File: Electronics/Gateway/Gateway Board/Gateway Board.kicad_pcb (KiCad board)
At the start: 2 copper layers, 110 parts, among them IC1 STM32H723ZGT6, IC2 TJA1057GT/3, IC3 TJA1057GT/3, IC4 TJA1057GT/3, IC5 TPS54295PWPR, IC6 LAN8742A-CZ-TR, J1 TYPE-C-31-M-12, J10 Conn_01x02_Pin, J11 Conn_01x02_Pin, J2 Screw_Terminal_01x02, J3 TC2030, J4 HR913129A, J5 Screw_Terminal_01x02, J6 Screw_Terminal_01x02, J7 MEM2075-00-140-01-A, J8 Screw_Terminal_01x02, J9 Conn_01x02_Pin, SW1 SW_DIP_x02, U1 USBLC6-4SC6-ES, U2 USBLC6-4SC6-ES, U3 USBLC6-4SC6-ES, X1 25MHz_Clock, X2 32.768kHz_Clock, X3 25MHz_Clock

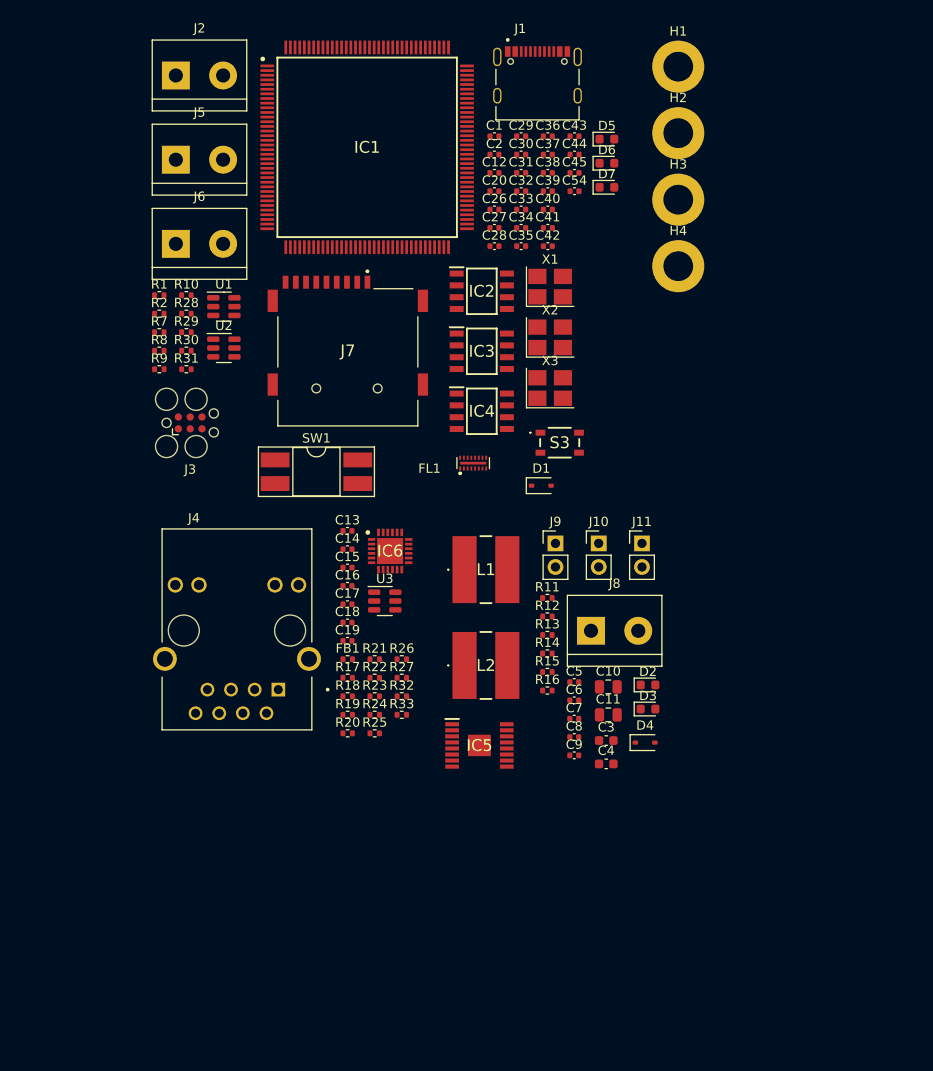
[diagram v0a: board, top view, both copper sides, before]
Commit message: Gateway board layout complete and routing begun
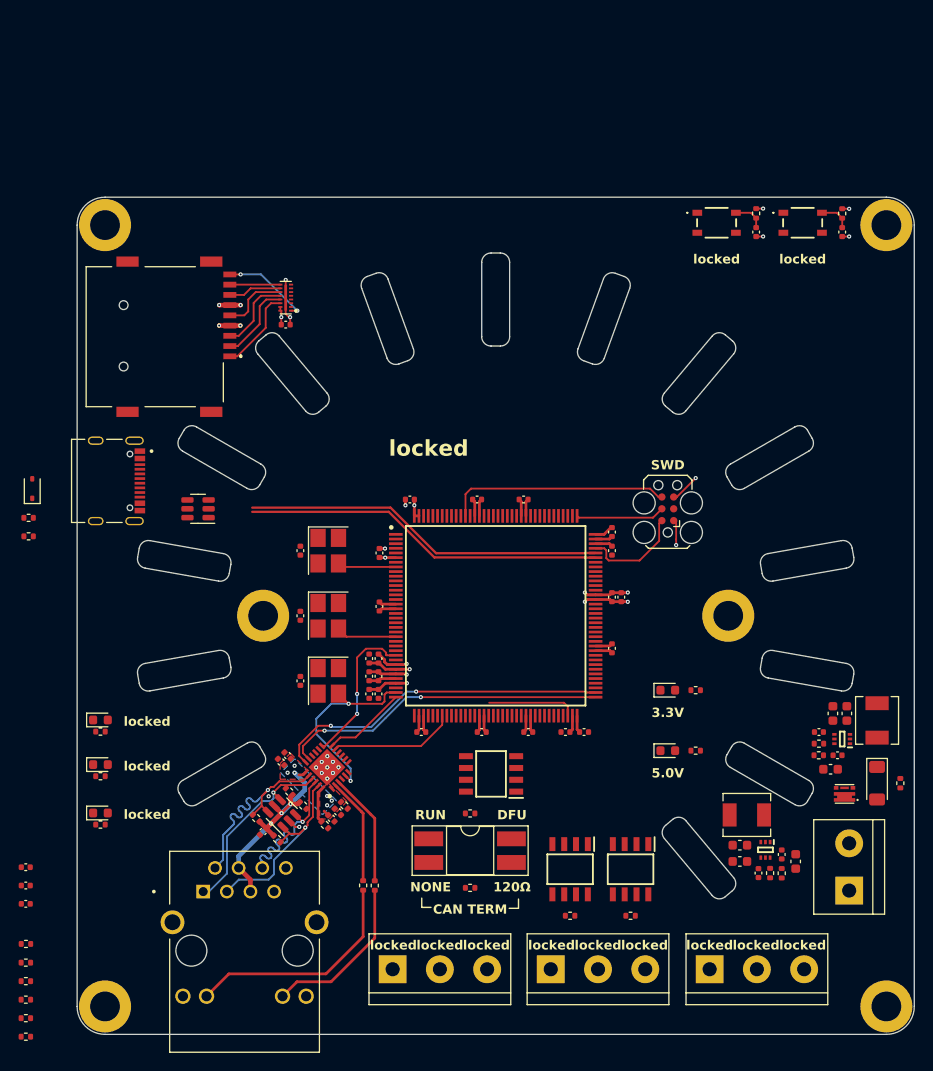
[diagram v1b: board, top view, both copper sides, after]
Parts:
- removed C1, C12, C13, C14, C18, C19, C2, C28, C30, C32, C33, C34, C35, C36, C37, C39, C40, C41, C42, C43, C44, C7, C8: 100n, Capacitor_SMD:C_0402_1005Metric
- removed C10, C11: 47u, Capacitor_SMD:C_0805_2012Metric
- removed C15, C20, C38, C45: 10u, Capacitor_SMD:C_0402_1005Metric
- removed C16, C29, C31, C9: 1u, Capacitor_SMD:C_0402_1005Metric
- removed C17: 470p, Capacitor_SMD:C_0402_1005Metric
- removed C26, C27: 2u2, Capacitor_SMD:C_0402_1005Metric
- removed C3, C4: 10u, Capacitor_SMD:C_0603_1608Metric
- removed C5, C54, C6: 10n, Capacitor_SMD:C_0402_1005Metric
- removed D1, D4: BAT760-115, Diode_SMD:D_SOD-323
- removed D2, D3, D6: Green, LED_SMD:LED_0603_1608Metric
- removed D5: Red, LED_SMD:LED_0603_1608Metric
- removed D7: Blue, LED_SMD:LED_0603_1608Metric
- removed FB1: 120R@100MHz, Resistor_SMD:R_0402_1005Metric
- removed FL1: EMIF06-MSD02N16, footprints:EMIF06MSD02N16
- removed H1, H2, H3, H4: MountingHole_Pad, MountingHole:MountingHole_3.2mm_M3_DIN965_Pad
- removed IC1: STM32H723ZGT6, MSL Footprints:QFP50P2200X2200X160-144N
- removed IC2, IC3, IC4: TJA1057GT/3, MSL Footprints:SOIC127P600X175-8N
- removed IC5: TPS54295PWPR, MSL Footprints:SOP65P640X120-17N
- removed IC6: LAN8742A-CZ-TR, MSL Footprints:QFN50P400X400X100-25N-D
- removed J1: TYPE-C-31-M-12, MSL Footprints:HRO_TYPE-C-31-M-12
- removed J10, J11, J9: Conn_01x02_Pin, Connector_PinHeader_2.54mm:PinHeader_1x02_P2.54mm_Vertical
- removed J2, J5, J6, J8: Screw_Terminal_01x02, TerminalBlock:TerminalBlock_bornier-2_P5.08mm
- removed J3: TC2030, Connector:Tag-Connect_TC2030-IDC-FP_2x03_P1.27mm_Vertical
- removed J4: HR913129A, MSL Footprints:HANRUN_HR913129A
- removed J7: MEM2075-00-140-01-A, MSL Footprints:MEM20750014001A
- removed L1: 3u3, MSL Footprints:29332C
- removed L2: 2u2, MSL Footprints:29222C
- removed R1, R2, R9: 120R, Resistor_SMD:R_0402_1005Metric
- removed R10, R14, R22, R25, R26, R27, R28, R33: 10k, Resistor_SMD:R_0402_1005Metric
- removed R11: 124k, Resistor_SMD:R_0402_1005Metric
- removed R12: 22k1, Resistor_SMD:R_0402_1005Metric
- removed R13: 33k, Resistor_SMD:R_0402_1005Metric
- removed R15: 2k2, Resistor_SMD:R_0402_1005Metric
- removed R16, R29, R30, R31, R32: 1k5, Resistor_SMD:R_0402_1005Metric
- removed R17, R18, R19, R20: 49R9, Resistor_SMD:R_0402_1005Metric
- removed R21: 12k1, Resistor_SMD:R_0402_1005Metric
- removed R23, R24: 330R, Resistor_SMD:R_0402_1005Metric
- removed R7, R8: 5k1, Resistor_SMD:R_0402_1005Metric
- removed S3: TS20-42-25-WT-160-SMT-TR, MSL Footprints:TS204225WT160SMTTRMSL
- removed SW1: SW_DIP_x02, Package_DIP:DIP-4_W8.89mm_SMDSocket_LongPads
- removed U1, U2, U3: USBLC6-4SC6-ES, Package_TO_SOT_SMD:SOT-23-6
- removed X1, X3: 25MHz_Clock, Oscillator:Oscillator_SMD_Abracon_ASE-4Pin_3.2x2.5mm_HandSoldering
- removed X2: 32.768kHz_Clock, Oscillator:Oscillator_SMD_Abracon_ASE-4Pin_3.2x2.5mm_HandSoldering
- added C201: 22u, Capacitor_SMD:C_0603_1608Metric, F.Cu at (177.2, 126.4)
- added C202: 22u, Capacitor_SMD:C_0603_1608Metric, F.Cu at (181.0, 116.5)
- added C203: 100n, Capacitor_SMD:C_0402_1005Metric, F.Cu at (175.8, 125.7)
- added C204: 100n, Capacitor_SMD:C_0402_1005Metric, F.Cu at (181.8, 115.0)
- added C205: 100n, Capacitor_SMD:C_0402_1005Metric, F.Cu at (173.2, 127.7)
- added C206: 100n, Capacitor_SMD:C_0402_1005Metric, F.Cu at (179.8, 112.5)
- added C207: 22u, Capacitor_SMD:C_0603_1608Metric, F.Cu at (171.2, 124.7)
- added C208: 22u, Capacitor_SMD:C_0603_1608Metric, F.Cu at (182.8, 110.5)
- added C209: 22u, Capacitor_SMD:C_0603_1608Metric, F.Cu at (171.2, 126.4)
- added C210: 22u, Capacitor_SMD:C_0603_1608Metric, F.Cu at (181.2, 110.5)
- added C301: 100n, Capacitor_SMD:C_0402_1005Metric, F.Cu at (124.0, 93.0)
- added C302: 100n, Capacitor_SMD:C_0402_1005Metric, F.Cu at (124.0, 100.0)
- added C303: 100n, Capacitor_SMD:C_0402_1005Metric, F.Cu at (124.0, 107.0)
- added C304: 10n, Capacitor_SMD:C_0402_1005Metric, F.Cu at (182.2, 58.8)
- added C305: 100n, Capacitor_SMD:C_0402_1005Metric, F.Cu at (132.4, 106.5)
- added C306: 1u, Capacitor_SMD:C_0402_1005Metric, F.Cu at (131.4, 106.5)
- added C307: 100n, Capacitor_SMD:C_0402_1005Metric, F.Cu at (135.8, 87.5)
- added C308: 100n, Capacitor_SMD:C_0402_1005Metric, F.Cu at (132.4, 108.4)
- added C309: 100n, Capacitor_SMD:C_0402_1005Metric, F.Cu at (157.5, 98.0)
- added C310: 1u, Capacitor_SMD:C_0402_1005Metric, F.Cu at (131.4, 108.4)
- added C311: 100n, Capacitor_SMD:C_0402_1005Metric, F.Cu at (132.5, 93.2)
- added C312: 100n, Capacitor_SMD:C_0402_1005Metric, F.Cu at (132.5, 99.0)
- added C313: 100n, Capacitor_SMD:C_0402_1005Metric, F.Cu at (137.0, 112.5)
- added C314: 100n, Capacitor_SMD:C_0402_1005Metric, F.Cu at (132.4, 104.6)
- added C315: 10u, Capacitor_SMD:C_0402_1005Metric, F.Cu at (158.5, 98.0)
- added C316: 100n, Capacitor_SMD:C_0402_1005Metric, F.Cu at (157.5, 91.0)
- added C317: 100n, Capacitor_SMD:C_0402_1005Metric, F.Cu at (154.5, 112.5)
- added C318: 100n, Capacitor_SMD:C_0402_1005Metric, F.Cu at (148.5, 112.5)
- added C319: 100n, Capacitor_SMD:C_0402_1005Metric, F.Cu at (143.5, 112.5)
- added C320: 100n, Capacitor_SMD:C_0402_1005Metric, F.Cu at (143.0, 87.5)
- added C321: 100n, Capacitor_SMD:C_0402_1005Metric, F.Cu at (148.0, 87.5)
- added C322: 10u, Capacitor_SMD:C_0402_1005Metric, F.Cu at (131.4, 104.6)
- added C323: 2u2, Capacitor_SMD:C_0402_1005Metric, F.Cu at (152.5, 112.5)
- added C324: 2u2, Capacitor_SMD:C_0402_1005Metric, F.Cu at (157.5, 93.0)
- added C325: 10u, Capacitor_SMD:C_0402_1005Metric, F.Cu at (122.4, 68.7)
- added C326: 10n, Capacitor_SMD:C_0402_1005Metric, F.Cu at (173.0, 58.8)
- added C327: 100n, Capacitor_SMD:C_0402_1005Metric, F.Cu at (157.5, 103.5)
- added C401: 100n, Capacitor_SMD:C_0402_1005Metric, F.Cu at (94.5, 127.0)
- added C402: 1u, Capacitor_SMD:C_0402_1005Metric, F.Cu at (94.5, 129.0)
- added C403: 470p, Capacitor_SMD:C_0402_1005Metric, F.Cu at (94.5, 131.0)
- added C404: 100n, Capacitor_SMD:C_0402_1005Metric, F.Cu at (121.9, 115.7)
- added C405: 100n, Capacitor_SMD:C_0402_1005Metric, F.Cu at (127.3, 121.8)
- added C406: 100n, Capacitor_SMD:C_0402_1005Metric, F.Cu at (122.6, 115.0)
- added C407: 10u, Capacitor_SMD:C_0402_1005Metric, F.Cu at (128.0, 121.1)
- added C408: 100n, Capacitor_SMD:C_0402_1005Metric, F.Cu at (120.0, 123.2)
- added D201: GREEN, LED_SMD:LED_0603_1608Metric, F.Cu at (163.5, 114.5)
- added D202: GREEN, LED_SMD:LED_0603_1608Metric, F.Cu at (163.5, 108.0)
- added D204: ZMM10V, Diode_SMD:D_MiniMELF, F.Cu at (186.0, 118.0)
- added D301: Red, LED_SMD:LED_0603_1608Metric, F.Cu at (102.5, 116.0)
- added D302: Green, LED_SMD:LED_0603_1608Metric, F.Cu at (102.5, 111.2)
- added D303: Blue, LED_SMD:LED_0603_1608Metric, F.Cu at (102.5, 121.2)
- added D304: BAT760-115, Diode_SMD:D_SOD-323, F.Cu at (95.2, 86.3)
- added FB401: 120R@100MHz, Resistor_SMD:R_0402_1005Metric, F.Cu at (128.7, 120.4)
- added FL301: EMIF06-MSD02N16, MSL Footprints:EMIF06MSD02N16, F.Cu at (122.6, 65.8)
- added G***: LOGO, MSL Footprints:ICRS_50mm, B.Cu at (145.0, 100.0)
- added H101: MountingHole_Pad, MountingHole:MountingHole_3.2mm_M3_DIN965_Pad, F.Cu at (103.0, 58.0)
- added H102: MountingHole_Pad, MountingHole:MountingHole_3.2mm_M3_DIN965_Pad, F.Cu at (103.0, 142.0)
- added H103: MountingHole_Pad, MountingHole:MountingHole_3.2mm_M3_DIN965_Pad, F.Cu at (187.0, 58.0)
- added H104: MountingHole_Pad, MountingHole:MountingHole_3.2mm_M3_DIN965_Pad, F.Cu at (187.0, 142.0)
- added H105: MountingHole_Pad, MountingHole:MountingHole_3.2mm_M3_DIN965_Pad, F.Cu at (120.0, 100.0)
- added H106: MountingHole_Pad, MountingHole:MountingHole_3.2mm_M3_DIN965_Pad, F.Cu at (170.0, 100.0)
- added IC201: TPS563202DRLR, MSL Footprints:SOTFL50P160X60-6N, F.Cu at (174.0, 125.2)
- added IC202: TPS563202DRLR, MSL Footprints:SOTFL50P160X60-6N, F.Cu at (182.2, 113.2)
- added IC301: STM32H723ZGT6, MSL Footprints:QFP50P2200X2200X160-144N, F.Cu at (145.0, 100.0)
- added IC302: TJA1057GT/3, MSL Footprints:SOIC127P600X175-8N, F.Cu at (144.5, 117.0)
- added IC303: TJA1057GT/3, MSL Footprints:SOIC127P600X175-8N, F.Cu at (153.0, 127.2)
- added IC304: TJA1057GT/3, MSL Footprints:SOIC127P600X175-8N, F.Cu at (159.5, 127.2)
- added IC401: LAN8742A-CZ-TR, MSL Footprints:QFN50P400X400X100-25N-D, F.Cu at (126.9, 116.3)
- added J201: Pluggable_Terminal_01x02, MSL Footprints:Pluggable_terminal-2_P5.08mm, F.Cu at (183.0, 129.5)
- added J301: TC2030, MSL Footprints:Tag-Connect_TC2030-IDC-FP_2x03_P1.27mm_Vertical, F.Cu at (163.5, 88.5)
- added J302: MEM2075-00-140-01-A, MSL Footprints:MEM20750014001A, F.Cu at (108.7, 70.0)
- added J303: TYPE-C-31-M-12, MSL Footprints:HRO_TYPE-C-31-M-12, F.Cu at (102.0, 85.5)
- added J304: Pluggable_Terminal_01x03, MSL Footprints:Pluggable_terminal-3_P5.08mm, F.Cu at (133.9, 138.0)
- added J305: Pluggable_Terminal_01x03, MSL Footprints:Pluggable_terminal-3_P5.08mm, F.Cu at (150.9, 138.0)
- added J306: Pluggable_Terminal_01x03, MSL Footprints:Pluggable_terminal-3_P5.08mm, F.Cu at (168.0, 138.0)
- added J401: HR913129A, MSL Footprints:HANRUN_HR913129A, F.Cu at (118.0, 136.0)
- added L201: 4u7, Inductor_SMD:L_Chilisin_BMRA00040420, F.Cu at (172.0, 121.4)
- added L202: 3u3, Inductor_SMD:L_Chilisin_BMRA00040420, F.Cu at (186.0, 111.2)
- added Q201: DMP3028LFDE, MSL Footprints:DMP2066UFDE7, F.Cu at (182.5, 119.2)
- added R201: 52k, Resistor_SMD:R_0402_1005Metric, F.Cu at (174.5, 127.7)
- added R202: 10k, Resistor_SMD:R_0402_1005Metric, F.Cu at (175.8, 127.7)
- added R203: 31k, Resistor_SMD:R_0402_1005Metric, F.Cu at (179.8, 113.8)
- added R204: 10k, Resistor_SMD:R_0402_1005Metric, F.Cu at (179.7, 115.0)
- added R205: 2k2, Resistor_SMD:R_0402_1005Metric, F.Cu at (166.5, 114.5)
- added R206: 1k5, Resistor_SMD:R_0402_1005Metric, F.Cu at (166.5, 108.0)
- added R207: 4k7, Resistor_SMD:R_0402_1005Metric, F.Cu at (188.5, 118.0)
- added R301: 1k5, Resistor_SMD:R_0402_1005Metric, F.Cu at (102.5, 117.2)
- added R302: 120R, Resistor_SMD:R_0402_1005Metric, F.Cu at (142.2, 129.2)
- added R303: 1k5, Resistor_SMD:R_0402_1005Metric, F.Cu at (102.5, 112.5)
- added R304: 1k5, Resistor_SMD:R_0402_1005Metric, F.Cu at (102.5, 122.5)
- added R305: 10k, Resistor_SMD:R_0402_1005Metric, F.Cu at (182.2, 56.8)
- added R306: 10k, Resistor_SMD:R_0402_1005Metric, F.Cu at (142.2, 121.2)
- added R307: 120R, Resistor_SMD:R_0402_1005Metric, F.Cu at (153.0, 132.2)
- added R308: 5k1, Resistor_SMD:R_0402_1005Metric, F.Cu at (94.8, 89.5)
- added R309: 5k1, Resistor_SMD:R_0402_1005Metric, F.Cu at (94.8, 91.5)
- added R310: 120R, Resistor_SMD:R_0402_1005Metric, F.Cu at (159.5, 132.2)
- added R311: 10k, Resistor_SMD:R_0402_1005Metric, F.Cu at (173.0, 56.7)
- added R401: 10k, Resistor_SMD:R_0402_1005Metric, F.Cu at (94.5, 135.3)
- added R402: 10k, Resistor_SMD:R_0402_1005Metric, F.Cu at (94.5, 137.3)
- added R403: 10k, Resistor_SMD:R_0402_1005Metric, F.Cu at (94.5, 139.3)
- added R404: 10k, Resistor_SMD:R_0402_1005Metric, F.Cu at (94.5, 141.3)
- added R405: 1k5, Resistor_SMD:R_0402_1005Metric, F.Cu at (94.5, 143.3)
- added R406: 10k, Resistor_SMD:R_0402_1005Metric, F.Cu at (94.5, 145.2)
- added R407: 12k1, Resistor_SMD:R_0402_1005Metric, F.Cu at (126.6, 122.5)
- added R408: 49R9, Resistor_SMD:R_0402_1005Metric, F.Cu at (122.8, 118.9)
- added R409: 49R9, Resistor_SMD:R_0402_1005Metric, F.Cu at (119.2, 121.8)
- added R410: 49R9, Resistor_SMD:R_0402_1005Metric, F.Cu at (121.5, 124.0)
- added R411: 49R9, Resistor_SMD:R_0402_1005Metric, F.Cu at (124.3, 120.4)
- added R412: 330R, Resistor_SMD:R_0402_1005Metric, F.Cu at (130.8, 129.0)
- added R413: 330R, Resistor_SMD:R_0402_1005Metric, F.Cu at (132.0, 129.0)
- added S301: TS20-42-25-WT-160-SMT-TR, MSL Footprints:TS204225WT160SMTTRMSL, F.Cu at (178.0, 57.8)
- added S302: TS20-42-25-WT-160-SMT-TR, MSL Footprints:TS204225WT160SMTTRMSL, F.Cu at (168.8, 57.8)
- added SW301: SW_DIP_x02, Package_DIP:DIP-4_W8.89mm_SMDSocket_LongPads, F.Cu at (142.2, 125.2)
- added U302: USBLC6-4SC6-ES, Package_TO_SOT_SMD:SOT-23-6, F.Cu at (113.0, 88.5)
- added U401: USBLC6-4SC6-ES, Package_TO_SOT_SMD:SOT-23-6, F.Cu at (122.0, 121.2)
- added X301: 50MHz_Clock, Oscillator:Oscillator_SMD_Abracon_ASE-4Pin_3.2x2.5mm_HandSoldering, F.Cu at (127.0, 107.0)
- added X302: 25MHz_Clock, Oscillator:Oscillator_SMD_Abracon_ASE-4Pin_3.2x2.5mm_HandSoldering, F.Cu at (127.0, 100.0)
- added X303: 32.768kHz_Clock, Oscillator:Oscillator_SMD_Abracon_ASE-4Pin_3.2x2.5mm_HandSoldering, F.Cu at (127.0, 93.0)
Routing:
- net +3.3V: track 0.00 -> 43.2 mm, vias 0 -> 12
- net GND: track 0.00 -> 42.2 mm, vias 0 -> 24
- net USB_DP: track 0.00 -> 39.0 mm
- net USB_DN: track 0.00 -> 39.0 mm
- net ETH_TXD1: track 0.00 -> 36.6 mm, vias 0 -> 2
- net ETH_TXD0: track 0.00 -> 35.3 mm, vias 0 -> 2
- net +3.3VA: track 0.00 -> 27.2 mm, vias 0 -> 9
- net /Ethernet/G_K: track 0.00 -> 24.5 mm
- net SWO: track 0.00 -> 24.1 mm
- net /Ethernet/TXN: track 0.00 -> 23.9 mm, vias 0 -> 1
- net /Ethernet/RXP: track 0.00 -> 21.8 mm, vias 0 -> 1
- net ETH_REF_CLK: track 0.00 -> 20.7 mm, vias 0 -> 2
- net /Ethernet/TXP: track 0.00 -> 20.6 mm, vias 0 -> 1
- net /Ethernet/RXN: track 0.00 -> 17.9 mm, vias 0 -> 1
- net /Ethernet/Y_K: track 0.00 -> 17.6 mm
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- added copper zone on B.Cu, net +3.3VA
- added copper zone on F.Cu, net +3.3VA
- added copper zone on In1.Cu, net GND
- added copper zone on In2.Cu, net GND
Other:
- board outline added: 90 x 90 mm
- copper layers 2 -> 4
- board text added: "120Ω"
- board text added: "3.3V"
- board text added: "5.0V"
- board text added: "CAN TERM"
- board text added: "DFU"
- board text added: "NONE"
- board text added: "RUN"
- board text added: "SWD"
- board text added: "locked"

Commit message: Sensor hub board done
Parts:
- added C1: 100n, Capacitor_SMD:C_0402_1005Metric, F.Cu at (140.2, 115.8)
- added C2: 100n, Capacitor_SMD:C_0402_1005Metric, F.Cu at (148.8, 117.0)
- added C3: 100n, Capacitor_SMD:C_0402_1005Metric, F.Cu at (150.5, 131.5)
- added C4: 100n, Capacitor_SMD:C_0402_1005Metric, F.Cu at (153.0, 123.0)
- added C5: 100n, Capacitor_SMD:C_0402_1005Metric, F.Cu at (157.0, 131.5)
- added C6: 100n, Capacitor_SMD:C_0402_1005Metric, F.Cu at (159.5, 123.0)
- added G***: LOGO, MSL Footprints:DC_logo_4mm, B.Cu at (187.3, 129.7)
- moved R405 49.8 mm to (132.2, 110.7)
- moved R404 49.0 mm to (134.5, 112.9)
- moved R403 47.3 mm to (135.7, 116.0), turned to 90 degrees
- moved R406 45.4 mm to (123.9, 110.6), turned to -135 degrees
- moved R402 44.9 mm to (133.1, 114.3), turned to -90 degrees
- moved R401 42.6 mm to (130.8, 113.0)
- moved C402 38.6 mm to (131.2, 117.1), turned to -45 degrees
- moved C401 38.6 mm to (130.8, 114.0), turned to 180 degrees
- moved C403 38.4 mm to (130.5, 117.8), turned to -45 degrees
- moved R306 33.9 mm to (138.7, 87.5)
- moved R308 18.5 mm to (113.0, 86.0)
- moved R309 18.2 mm to (113.0, 91.0)
- moved D304 11.1 mm to (103.5, 93.6)
- moved R302 3.25 mm to (139.0, 129.2)
- moved SW301 3.25 mm to (139.0, 125.2)
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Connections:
- IC301 pad 10: unconnected-(IC301-PF0-Pad10) -> LEDG
- IC301 pad 11: unconnected-(IC301-PF1-Pad11) -> LEDR
- IC301 pad 12: unconnected-(IC301-PF2-Pad12) -> LEDB
- IC301 pad 123: unconnected-(IC301-PD7-Pad123) -> BTN
- IC301 pad 13: unconnected-(IC301-PF3-Pad13) -> ETH_RST
- IC301 pad 14: unconnected-(IC301-PF4-Pad14) -> ETH_INT
- IC301 pad 47: unconnected-(IC301-PB1-Pad47) -> SILENT1
- IC301 pad 64: unconnected-(IC301-PE11-Pad64) -> SILENT2
- IC301 pad 65: unconnected-(IC301-PE12-Pad65) -> SILENT3
- J302 pad 10: GND -> unconnected-(J302-MP1-Pad10)
- J302 pad 11: GND -> unconnected-(J302-MP2-Pad11)
- J302 pad 12: GND -> unconnected-(J302-MP3-Pad12)
- J302 pad 13: GND -> unconnected-(J302-MP4-Pad13)
- J303 pad S2: unconnected-(J303-SHIELD-PadS1) -> unconnected-(J303-SHIELD-PadS2)
- J303 pad S3: unconnected-(J303-SHIELD-PadS1) -> unconnected-(J303-SHIELD-PadS3)
- J303 pad S4: unconnected-(J303-SHIELD-PadS1) -> unconnected-(J303-SHIELD-PadS4)
- R405 pad 2: ETH_MDC -> ETH_MDIO
- U302 pad 1: /Microcontroller/CC1 -> /Microcontroller/CC2
- U302 pad 3: /Microcontroller/CC2 -> /Microcontroller/CC1
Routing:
- net VIN: track 0.00 -> 150.3 mm, vias 0 -> 8
- net NRST: track 3.43 -> 95.2 mm, vias 0 -> 2
- net +3.3V: track 43.2 -> 119.7 mm, vias 12 -> 45
- net GND: track 42.2 -> 114.9 mm, vias 24 -> 97
- net SDMMC1_DAT0: track 0.00 -> 54.7 mm, vias 0 -> 2
- net SDMMC1_DAT1: track 0.00 -> 54.5 mm, vias 0 -> 2
- net LEDB: track 0.00 -> 53.1 mm
- net CAN_RX2: track 0.00 -> 52.7 mm, vias 0 -> 2
- net SDMMC1_CD: track 9.55 -> 61.0 mm, vias 2 -> 5
- net SDMMC1_CLK: track 0.00 -> 50.5 mm
- net CAN_TX2: track 0.00 -> 48.9 mm, vias 0 -> 2
- net LEDR: track 0.00 -> 48.3 mm
- net CAN_TX3: track 0.00 -> 48.2 mm, vias 0 -> 2
- net SDMMC1_DAT3: track 0.00 -> 48.2 mm
- net CAN_RX3: track 0.00 -> 47.2 mm, vias 0 -> 2
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- added copper zone on B.Cu, net +3.3V
- added copper zone on F.Cu, net +3.3V
- added copper zone on B.Cu, net +5V
- added copper zone on F.Cu, net +5V
- added copper zone on F.Cu, net /Power/3V3_SW
- added copper zone on F.Cu, net /Power/5V_SW
- added copper zone on F.Cu, net GND
- added copper zone on F.Cu, net VIN
- added copper zone on F.Cu, net VIN_RAW
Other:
- board text added: "+"
- board text added: "-"
- board text added: "Input: 5-16V 0.5A"
- board text removed: "3.3V"
- board text removed: "5.0V"

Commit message: Motor driver and power boards done
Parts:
- added REF**: ESD-Logo_8.9x8mm_SilkScreen, Symbol:ESD-Logo_8.9x8mm_SilkScreen, B.Cu at (111.8, 69.0)
- added REF**: WEEE-Logo_5.6x8mm_SilkScreen, Symbol:WEEE-Logo_5.6x8mm_SilkScreen, B.Cu at (177.8, 69.0)

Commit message: All boards done
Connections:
- H101 pad 1: GND -> unconnected-(H101-Pad1)
- H102 pad 1: GND -> unconnected-(H102-Pad1)
- H103 pad 1: GND -> unconnected-(H103-Pad1)
- H104 pad 1: GND -> unconnected-(H104-Pad1)
- H105 pad 1: GND -> unconnected-(H105-Pad1)
- H106 pad 1: GND -> unconnected-(H106-Pad1)
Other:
- board text removed: "+"
- board text removed: "-"
- board text removed: "120Ω"
- board text removed: "CAN TERM"
- board text removed: "DFU"
- board text removed: "Input: 5-16V 0.5A"
- board text removed: "NONE"
- board text removed: "RUN"
- board text removed: "SWD"

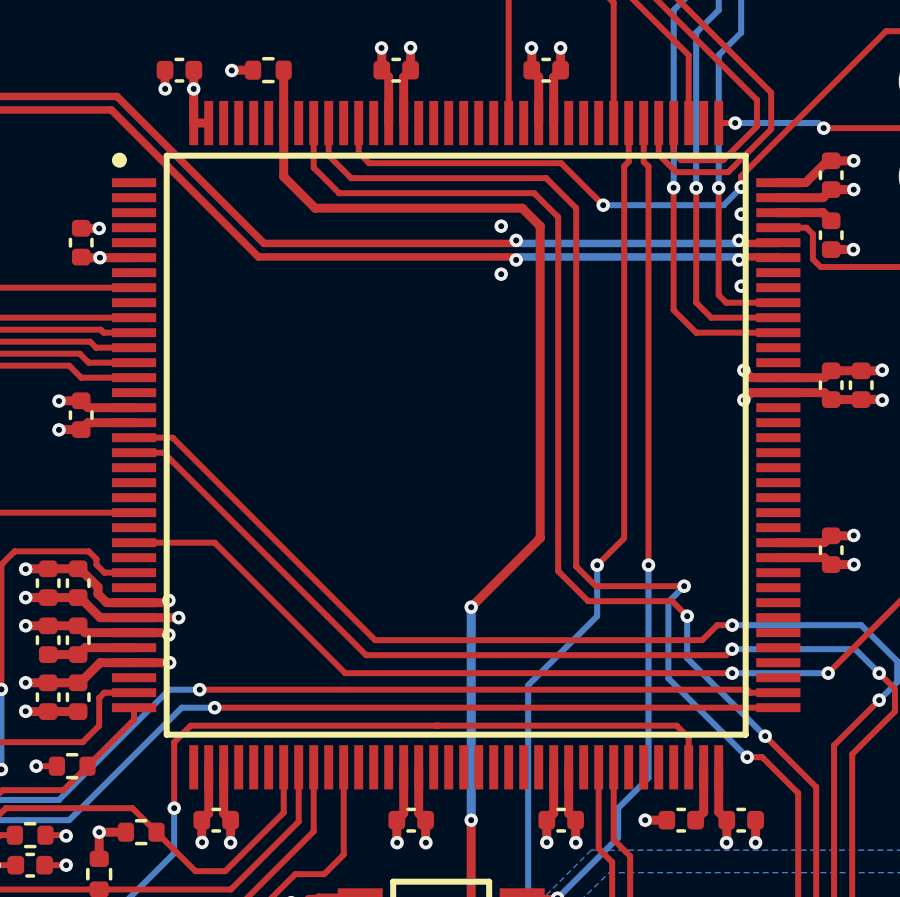
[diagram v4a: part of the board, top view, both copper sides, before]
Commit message: Tidied, added STM32 ethernet example, minor PCB changes
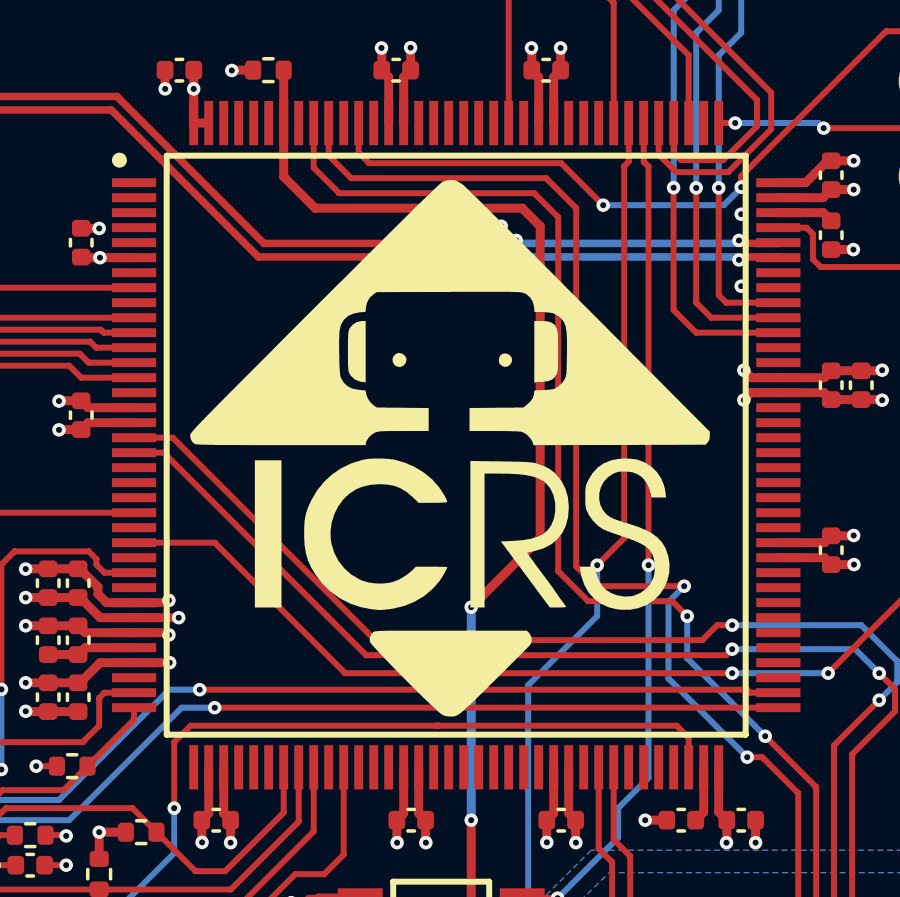
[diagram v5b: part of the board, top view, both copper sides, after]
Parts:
- added G***: LOGO, MSL Footprints:ICRS_20mm, F.Cu at (145.0, 100.0)
